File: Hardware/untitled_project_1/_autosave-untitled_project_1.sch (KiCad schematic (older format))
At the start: 1 part

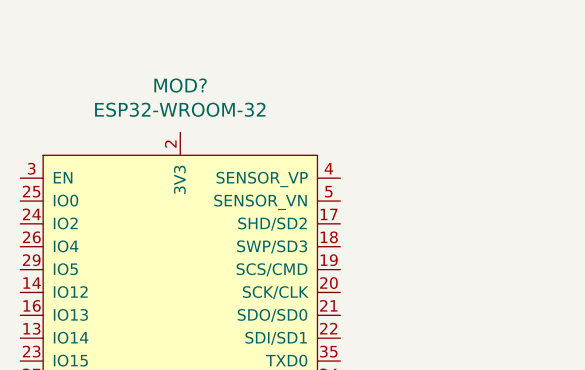
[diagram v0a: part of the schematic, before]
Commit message: routed 144led in array
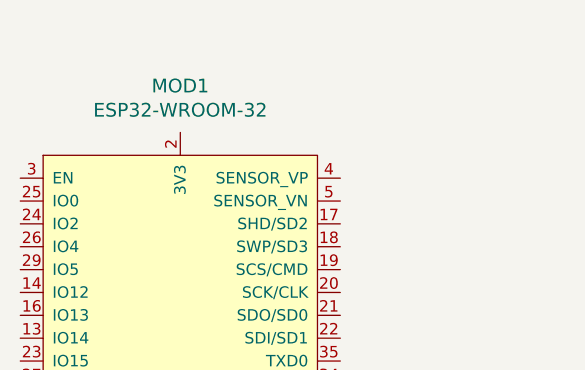
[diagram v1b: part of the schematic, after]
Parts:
- gave numbers to parts that had none: 1
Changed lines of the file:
@@
 $Descr A4 11693 8268
 encoding utf-8
-Sheet 1 3
+Sheet 1 4
 Title ""
 Date ""
@@
 $EndDescr
 $Comp
-L dk_RF-Transceiver-Modules:ESP32-WROOM-32 MOD?
+L dk_RF-Transceiver-Modules:ESP32-WROOM-32 MOD1
 U 1 1 5EF053D0
 P 2600 1600
-F 0 "MOD?" H 2800 1903 60  0000 C CNN
+F 0 "MOD1" H 2800 1903 60  0000 C CNN
 F 1 "ESP32-WROOM-32" H 2800 1797 60  0000 C CNN
 F 2 "digikey-footprints:ESP32-WROOM-32D" H 2800 1800 60  0001 L CNN
